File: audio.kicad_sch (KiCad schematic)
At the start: 6 parts, among them J2 AudioJack3, U4 PCM3060PWR

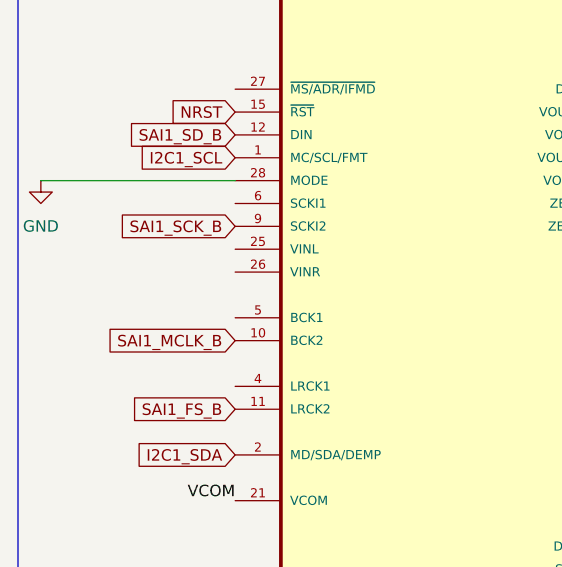
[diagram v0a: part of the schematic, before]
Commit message: fix swapped SAI clock signals
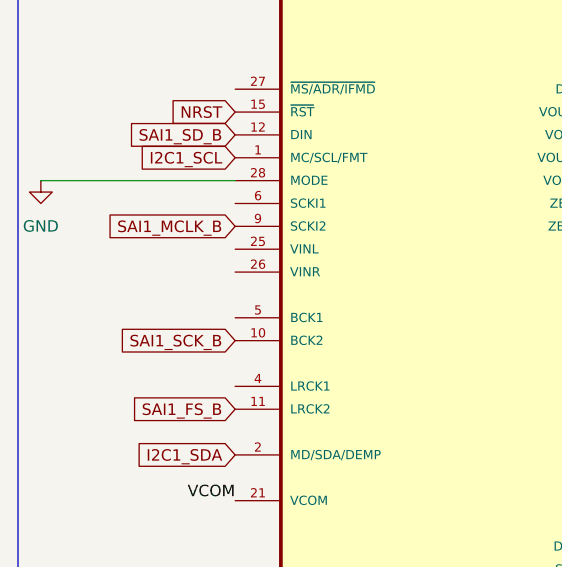
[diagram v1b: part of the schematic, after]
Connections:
- net SAI1_MCLK_B: now also U4.9 (SCKI2); no longer U4.10 (BCK2)
- net SAI1_SCK_B: now also U4.10 (BCK2); no longer U4.9 (SCKI2)
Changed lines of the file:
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@@
     )
   )
-  (global_label "SAI1_SCK_B" (shape input) (at 36.83 44.45 180) (fields_autoplaced)
+  (global_label "SAI1_SCK_B" (shape input) (at 36.83 57.15 180) (fields_autoplaced)
     (effects (font (size 1.27 1.27)) (justify right))
-    (property "Intersheetrefs" "${INTERSHEET_REFS}" (at 22.8571 44.45 0)
+    (property "Intersheetrefs" "${INTERSHEET_REFS}" (at 22.8571 57.15 0)
       (effects (font (size 1.27 1.27)) (justify right) hide)
     )
@@
     )
   )
-  (global_label "SAI1_MCLK_B" (shape input) (at 36.83 57.15 180) (fields_autoplaced)
+  (global_label "SAI1_MCLK_B" (shape input) (at 36.83 44.45 180) (fields_autoplaced)
     (effects (font (size 1.27 1.27)) (justify right))
-    (property "Intersheetrefs" "${INTERSHEET_REFS}" (at 21.5871 57.15 0)
+    (property "Intersheetrefs" "${INTERSHEET_REFS}" (at 21.5871 44.45 0)
       (effects (font (size 1.27 1.27)) (justify right) hide)
     )
